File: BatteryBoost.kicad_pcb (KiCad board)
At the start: 2 copper layers, 80 x 40 mm, 42 parts, among them J1 Mounting Hole, J2 Mounting Hole, J3 Mounting Hole, J4 Mounting Hole, J5 USB_B_Micro, J6 Battery, J7 Output, Q1 -40V 7.5A 2.5V @ 250uA 40mΩ @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, Q2 -40V 7.5A 2.5V @ 250uA 40mΩ @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, Q3 Q_PNP_BCE, SW1 SW_SPDT, U1 SP34063AEN, U2 TP4056

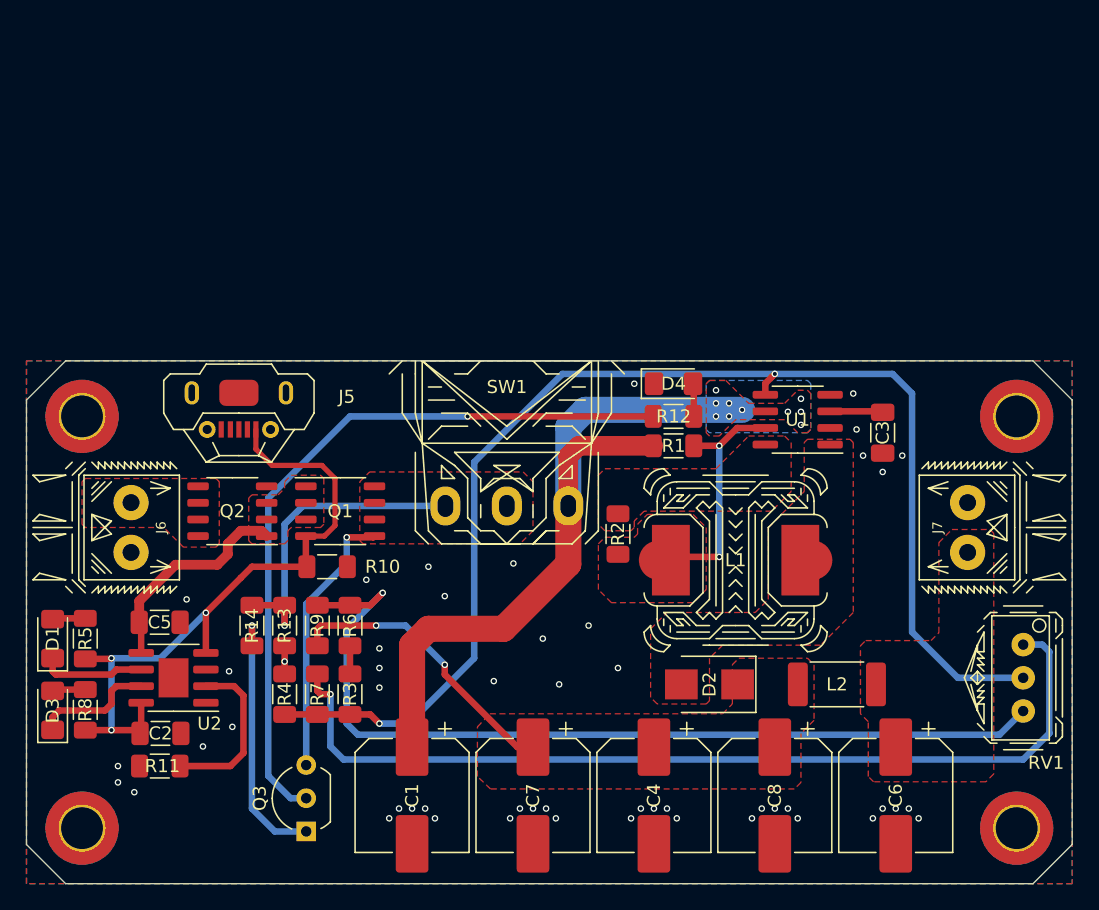
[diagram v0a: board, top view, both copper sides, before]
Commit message: Preliminary placement for protection circuit
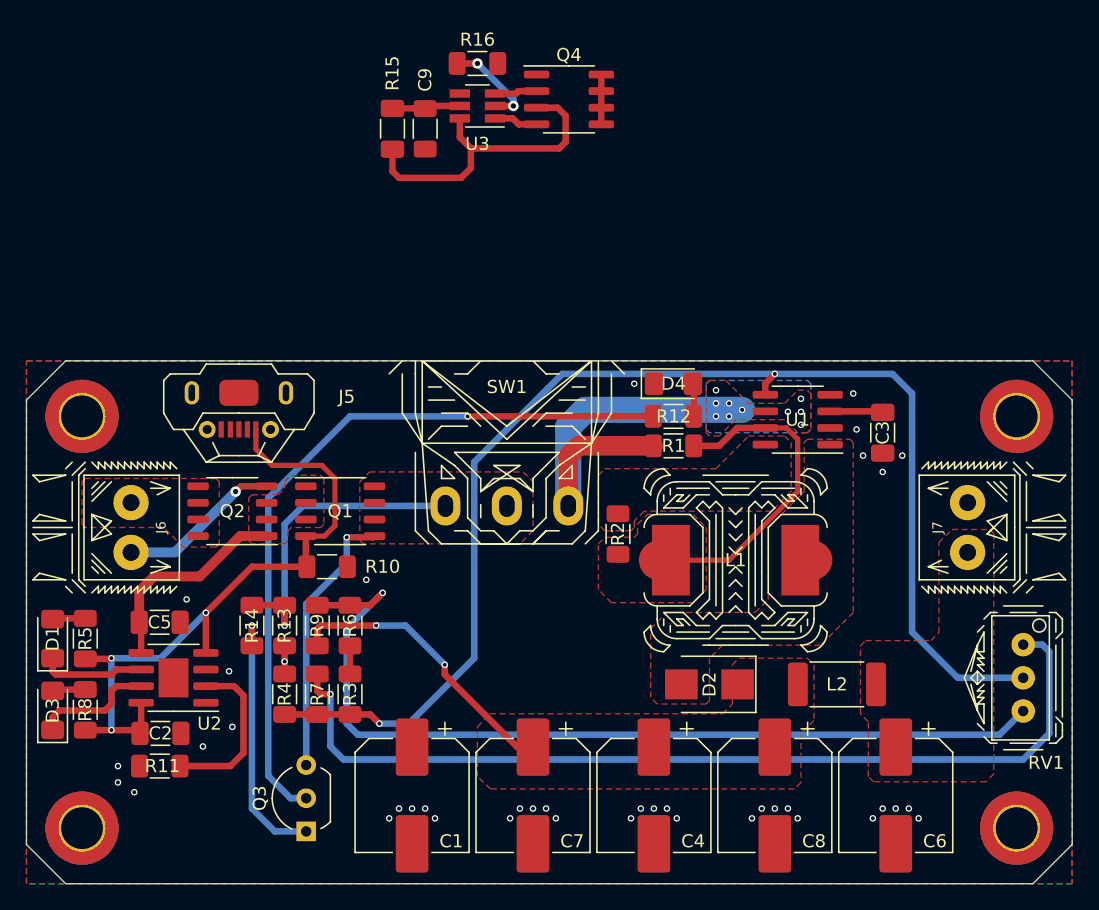
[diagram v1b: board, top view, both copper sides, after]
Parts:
- added C9: 100nF ±10% 50V X7R, Capacitor_SMD:C_1206_3216Metric_Pad1.33x1.80mm_HandSolder, F.Cu at (28.0, -17.8)
- added Q4: 20V 7.5A 24mΩ @ 2.5Vgs, Package_SO:SOIC-8_3.9x4.9mm_P1.27mm, F.Cu at (41.5, -20.0)
- added R15: 330R ±1% 0.25W, Resistor_SMD:R_1206_3216Metric_Pad1.30x1.75mm_HandSolder, F.Cu at (30.5, -17.8)
- added R16: 1.2kΩ ±1% 0.25W, Resistor_SMD:R_1206_3216Metric_Pad1.30x1.75mm_HandSolder, F.Cu at (34.5, -22.8)
- added U3: AP9101CK6, Package_TO_SOT_SMD:SOT-23-6_Handsoldering, F.Cu at (34.5, -19.5)
- Q2: value -40V 7.5A 2.5V @ 250uA 40mΩ @ 6A -> -40V 7.5A 40mΩ @ 6A
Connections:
- net Net-(J6-Pad1) renamed /Raw_Batt_+
- J6 pad 2: GND -> /Raw_Batt_-
- Q2 pad G: GND -> /Raw_Batt_-
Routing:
- net /Raw_Batt_-: track 0.00 -> 36.7 mm, vias 0 -> 1
- net SMPS_Pwr: track 57.3 -> 30.5 mm
- net Net-(R16-Pad1): track 0.00 -> 7.34 mm, vias 0 -> 2
- net Net-(L1-Pad2): track 18.3 -> 25.1 mm, vias 2 -> 0
- net Net-(C9-Pad1): track 0.00 -> 5.24 mm
- net Net-(Q4-Pad5): track 0.00 -> 3.81 mm
- net Net-(Q4-Pad4): track 0.00 -> 3.36 mm
- net Net-(Q4-Pad2): track 0.00 -> 3.25 mm
- net GND: vias 51 -> 40

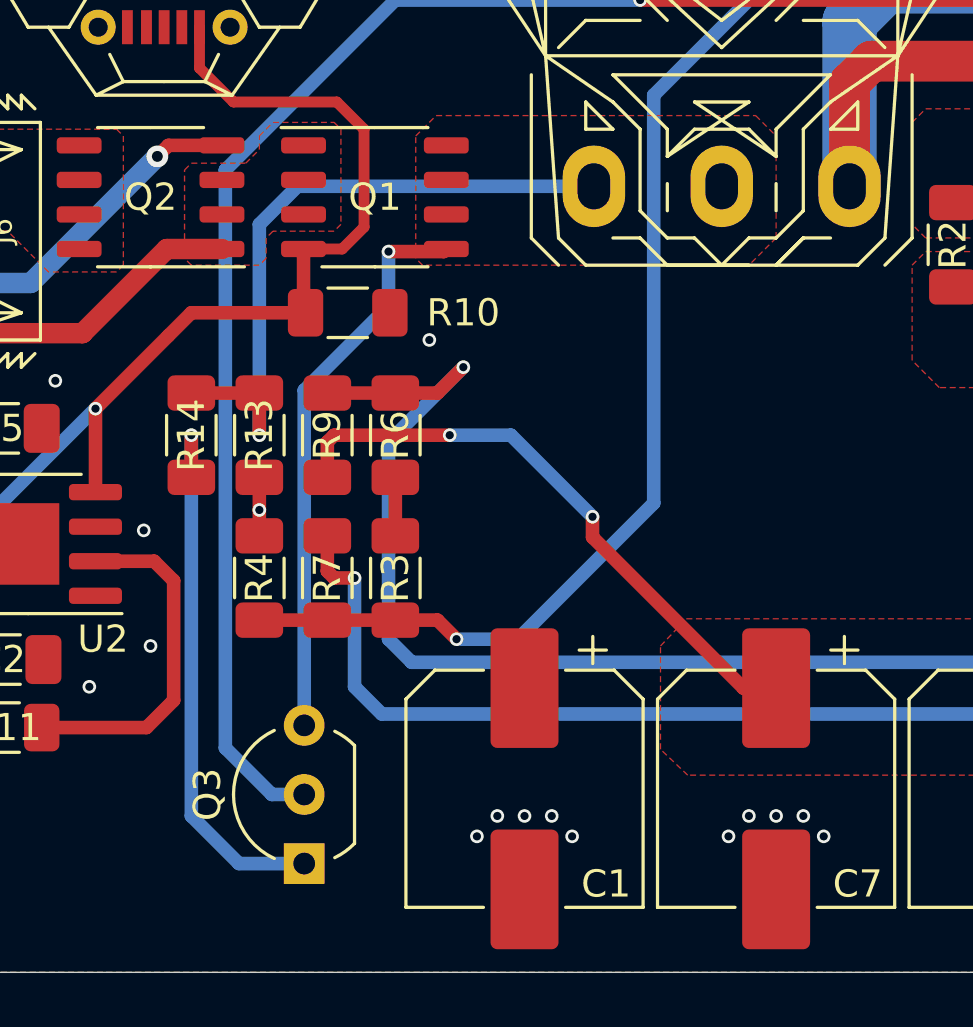
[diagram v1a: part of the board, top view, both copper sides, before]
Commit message: remove BJT circuit layout
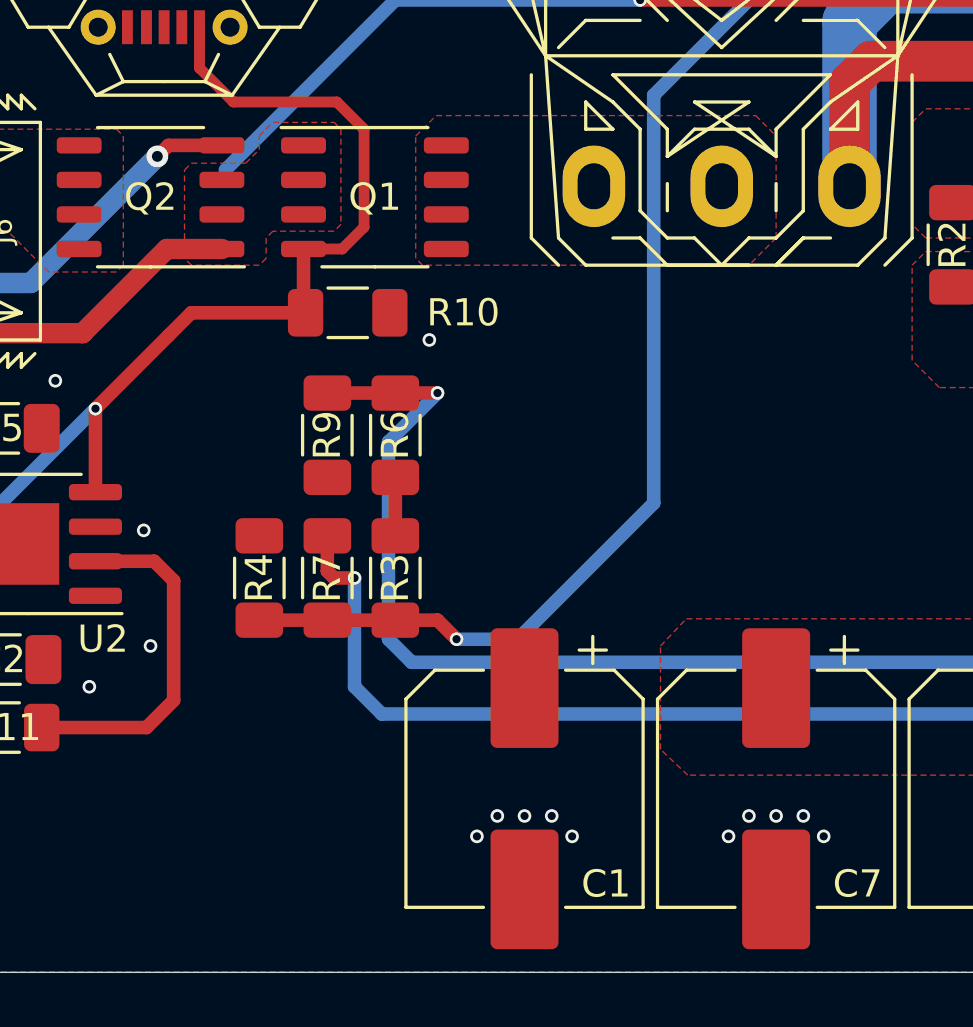
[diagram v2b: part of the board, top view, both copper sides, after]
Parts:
- removed Q3: Q_PNP_BCE, Package_TO_SOT_THT:TO-92_Inline_Wide
- removed R13, R14: 10k, Resistor_SMD:R_1206_3216Metric_Pad1.30x1.75mm_HandSolder
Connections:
- R12 pad 1: Net-(Q3-Pad2) -> SMPS_Pwr
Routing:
- net Net-(Q3-Pad2): track 56.9 -> 0.00 mm, vias 1 -> 0
- net SMPS_Pwr: track 30.5 -> 62.6 mm, vias 10 -> 11
- net Net-(SW1-Pad1): track 24.7 -> 0.00 mm, vias 1 -> 0
- net SMPS_Output: track 23.6 -> 0.00 mm, vias 2 -> 0
- net Net-(Q1-PadD): track 20.9 -> 0.00 mm, vias 1 -> 0
- net Net-(Q3-Pad1): track 20.4 -> 0.00 mm, vias 1 -> 0
- net Net-(R6-Pad2): track 69.4 -> 66.7 mm
- net GND: track 2.15 -> 0.00 mm, vias 40 -> 39

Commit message: Update net names
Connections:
- R11 pad 1: GND -> Net-(R11-Pad1)
- R11 pad 2: Net-(R11-Pad2) -> GND
- R8 pad 1: Net-(D3-Pad2) -> +5V
- R8 pad 2: +5V -> Net-(D3-Pad2)
- U2 pad 2: Net-(R11-Pad2) -> Net-(R11-Pad1)
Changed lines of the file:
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@@
     (zones 0)
     (modules 44)
-    (nets 33)
+    (nets 34)
   )
   (page A4)
@@
   (net 31 "Net-(R16-Pad1)")
   (net 32 "Net-(SW1-Pad1)")
+  (net 33 "Net-(R11-Pad1)")
   (net_class Default "This is the default net class."
     (clearance 0.2)
@@
     (add_net "Net-(Q4-Pad4)")
     (add_net "Net-(Q4-Pad5)")
+    (add_net "Net-(R11-Pad1)")
     (add_net "Net-(R11-Pad2)")
     (add_net "Net-(R16-Pad1)")
@@
       (net 1 GND))
     (pad 2 smd roundrect (at -2.475 -0.635 180) (size 1.95 0.6) (layers F.Cu F.Paste F.Mask) (roundrect_rratio 0.25)
-      (net 19 "Net-(R11-Pad2)"))
+      (net 33 "Net-(R11-Pad1)"))
     (pad 3 smd roundrect (at -2.475 0.635 180) (size 1.95 0.6) (layers F.Cu F.Paste F.Mask) (roundrect_rratio 0.25)
       (net 1 GND))
@@
     )
     (pad 1 smd roundrect (at -1.55 0) (size 1.3 1.75) (layers F.Cu F.Paste F.Mask) (roundrect_rratio 0.192308)
+      (net 33 "Net-(R11-Pad1)"))
+    (pad 2 smd roundrect (at 1.55 0) (size 1.3 1.75) (layers F.Cu F.Paste F.Mask) (roundrect_rratio 0.192308)
       (net 1 GND))
-    (pad 2 smd roundrect (at 1.55 0) (size 1.3 1.75) (layers F.Cu F.Paste F.Mask) (roundrect_rratio 0.192308)
-      (net 19 "Net-(R11-Pad2)"))
     (model ${KISYS3DMOD}/Resistor_SMD.3dshapes/R_1206_3216Metric.wrl
       (at (xyz 0 0 0))
@@
     )
     (pad 2 smd roundrect (at 1.55 0 270) (size 1.3 1.75) (layers F.Cu F.Paste F.Mask) (roundrect_rratio 0.192308)
+      (net 4 "Net-(D3-Pad2)"))
+    (pad 1 smd roundrect (at -1.55 0 270) (size 1.3 1.75) (layers F.Cu F.Paste F.Mask) (roundrect_rratio 0.192308)
       (net 2 +5V))
-    (pad 1 smd roundrect (at -1.55 0 270) (size 1.3 1.75) (layers F.Cu F.Paste F.Mask) (roundrect_rratio 0.192308)
-      (net 4 "Net-(D3-Pad2)"))
     (model ${KISYS3DMOD}/Resistor_SMD.3dshapes/R_1206_3216Metric.wrl
       (at (xyz 0 0 0))

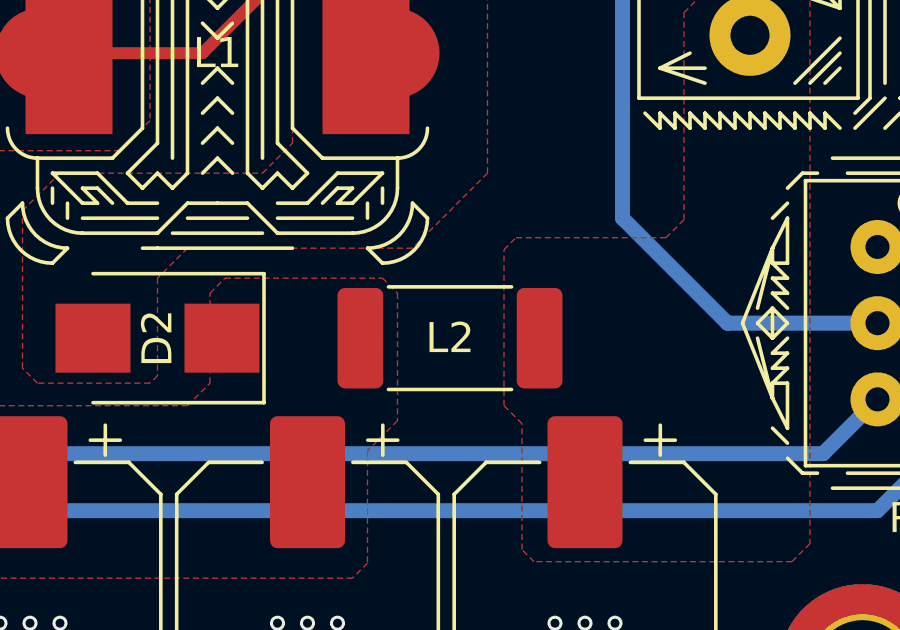
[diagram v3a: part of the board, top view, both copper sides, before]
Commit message: Add footprint for filter inductor
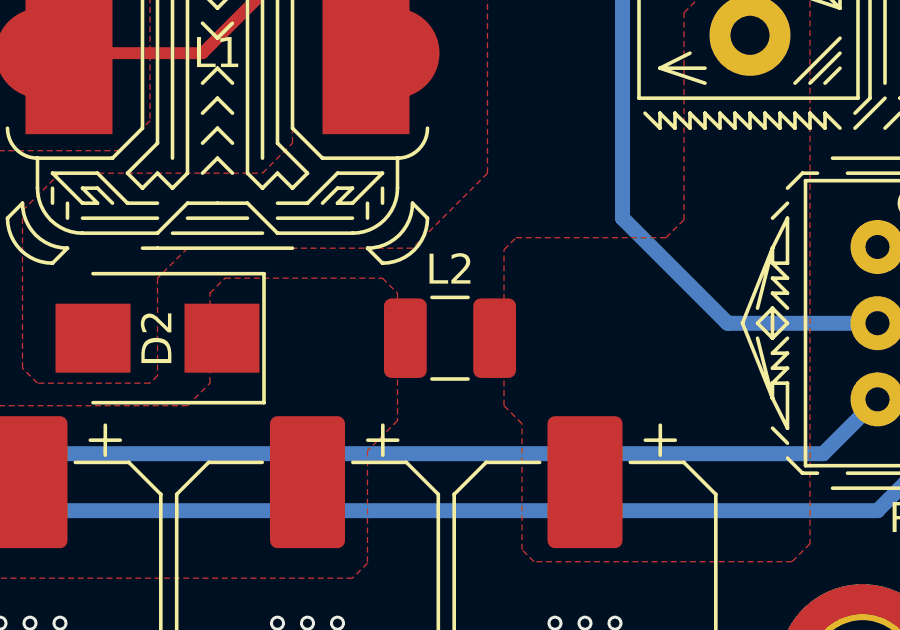
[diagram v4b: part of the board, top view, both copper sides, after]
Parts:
- L2: footprint Inductor_SMD:L_2512_6332Metric_Pad1.52x3.35mm_HandSolder -> Inductor_SMD:L_1210_3225Metric_Pad1.42x2.65mm_HandSolder
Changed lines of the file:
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@@
     (add_net VBATT)
+  )
+  (module Inductor_SMD:L_1210_3225Metric_Pad1.42x2.65mm_HandSolder (layer F.Cu)
+    (at 62 24.75)
+    (descr "Inductor SMD 1210 (3225 Metric), square (rectangular) end terminal, IPC_7351 nominal with elongated pad for handsoldering. (Body size source: http://www.tortai-tech.com/upload/download/2011102023233369053.pdf), generated with kicad-footprint-generator")
+    (tags "inductor handsolder")
+    (attr smd)
+    (fp_text reference L2 (at 0 -2.28) (layer F.SilkS)
+      (effects (font (size 1 1) (thickness 0.15)))
+    )
+    (fp_text value "1uH ±20% 3.29A 59mΩ" (at 0 2.28) (layer F.Fab)
+      (effects (font (size 1 1) (thickness 0.15)))
+    )
+    (fp_text user %R (at 0 0) (layer F.Fab)
+      (effects (font (size 0.8 0.8) (thickness 0.12)))
+    )
+    (fp_line (start -1.6 1.25) (end -1.6 -1.25) (layer F.Fab) (width 0.1))
+    (fp_line (start -1.6 -1.25) (end 1.6 -1.25) (layer F.Fab) (width 0.1))
+    (fp_line (start 1.6 -1.25) (end 1.6 1.25) (layer F.Fab) (width 0.1))
+    (fp_line (start 1.6 1.25) (end -1.6 1.25) (layer F.Fab) (width 0.1))
+    (fp_line (start -0.602064 -1.36) (end 0.602064 -1.36) (layer F.SilkS) (width 0.12))
+    (fp_line (start -0.602064 1.36) (end 0.602064 1.36) (layer F.SilkS) (width 0.12))
+    (fp_line (start -2.45 1.58) (end -2.45 -1.58) (layer F.CrtYd) (width 0.05))
+    (fp_line (start -2.45 -1.58) (end 2.45 -1.58) (layer F.CrtYd) (width 0.05))
+    (fp_line (start 2.45 -1.58) (end 2.45 1.58) (layer F.CrtYd) (width 0.05))
+    (fp_line (start 2.45 1.58) (end -2.45 1.58) (layer F.CrtYd) (width 0.05))
+    (pad 2 smd roundrect (at 1.4875 0) (size 1.425 2.65) (layers F.Cu F.Paste F.Mask) (roundrect_rratio 0.175439)
+      (net 21 /Vout))
+    (pad 1 smd roundrect (at -1.4875 0) (size 1.425 2.65) (layers F.Cu F.Paste F.Mask) (roundrect_rratio 0.175439)
+      (net 20 SMPS_Output))
+    (model ${KISYS3DMOD}/Inductor_SMD.3dshapes/L_1210_3225Metric.wrl
+      (at (xyz 0 0 0))
+      (scale (xyz 1 1 1))
+      (rotate (xyz 0 0 0))
+    )
   )
   (module Package_TO_SOT_SMD:SOT-23-6_Handsoldering (layer F.Cu)
@@
       (at (xyz 0 0 0))
       (scale (xyz 1 1 1))
-      (rotate (xyz 0 0 0))
-    )
-  )
-  (module Inductor_SMD:L_2512_6332Metric_Pad1.52x3.35mm_HandSolder (layer F.Cu)
-    (at 62 24.75)
-    (descr "Inductor SMD 2512 (6332 Metric), square (rectangular) end terminal, IPC_7351 nominal with elongated pad for handsoldering. (Body size source: http://www.tortai-tech.com/upload/download/2011102023233369053.pdf), generated with kicad-footprint-generator")
-    (tags "inductor handsolder")
-    (attr smd)
-    (fp_text reference L2 (at 0 0) (layer F.SilkS)
-      (effects (font (size 1 1) (thickness 0.15)))
-    )
-    (fp_text value "1uH ±20% 3.29A 59mΩ" (at 0 2.62) (layer F.Fab)
-      (effects (font (size 1 1) (thickness 0.15)))
-    )
-    (fp_line (start 4 1.92) (end -4 1.92) (layer F.CrtYd) (width 0.05))
-    (fp_line (start 4 -1.92) (end 4 1.92) (layer F.CrtYd) (width 0.05))
-    (fp_line (start -4 -1.92) (end 4 -1.92) (layer F.CrtYd) (width 0.05))
-    (fp_line (start -4 1.92) (end -4 -1.92) (layer F.CrtYd) (width 0.05))
-    (fp_line (start -2.052064 1.71) (end 2.052064 1.71) (layer F.SilkS) (width 0.12))
-    (fp_line (start -2.052064 -1.71) (end 2.052064 -1.71) (layer F.SilkS) (width 0.12))
-    (fp_line (start 3.15 1.6) (end -3.15 1.6) (layer F.Fab) (width 0.1))
-    (fp_line (start 3.15 -1.6) (end 3.15 1.6) (layer F.Fab) (width 0.1))
-    (fp_line (start -3.15 -1.6) (end 3.15 -1.6) (layer F.Fab) (width 0.1))
-    (fp_line (start -3.15 1.6) (end -3.15 -1.6) (layer F.Fab) (width 0.1))
-    (fp_text user %R (at 0 0) (layer F.Fab)
-      (effects (font (size 1 1) (thickness 0.15)))
-    )
-    (pad 2 smd roundrect (at 2.9875 0) (size 1.525 3.35) (layers F.Cu F.Paste F.Mask) (roundrect_rratio 0.163934)
-      (net 21 /Vout))
-    (pad 1 smd roundrect (at -2.9875 0) (size 1.525 3.35) (layers F.Cu F.Paste F.Mask) (roundrect_rratio 0.163934)
-      (net 20 SMPS_Output))
-    (model ${KISYS3DMOD}/Inductor_SMD.3dshapes/L_2512_6332Metric.wrl
-      (at (xyz 0 0 0))
-      (scale (xyz 1 1 1))
